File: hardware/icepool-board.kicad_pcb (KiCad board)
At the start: 4 copper layers, 152 x 96 mm, 120 parts, among them J1 USB_B_Micro, J10 Conn_02x08_Odd_Even, J11 Conn_02x08_Odd_Even, J12 Conn_02x08_Odd_Even, J13 Conn_02x08_Odd_Even, J14 Conn_02x08_Odd_Even, J15 Conn_02x08_Odd_Even, J16 Conn_02x08_Odd_Even, J17 Conn_02x08_Odd_Even, J18 Conn_02x08_Odd_Even, J19 Conn_02x08_Odd_Even, J2 Conn_01x02, J20 Conn_02x08_Odd_Even, J21 Conn_01x04, J3 PCIe_6pin, J4 Conn_02x08_Odd_Even, J5 Conn_02x08_Odd_Even, J6 Conn_02x08_Odd_Even, J7 Conn_02x08_Odd_Even, J8 Conn_02x08_Odd_Even, J9 Conn_02x08_Odd_Even, U1 FT232H, U2 AP7361C_SOT-89-5, U6 AP7361C_SOT-89-5, U7 AP7361C_SOT-89-5, U8 iCE40HX8K-BG121(121-Ball_caBG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, U9 AOZ2255LQI-30, X1 ASEM1-12.000MHZ, X2 ASEM1-12.000MHZ

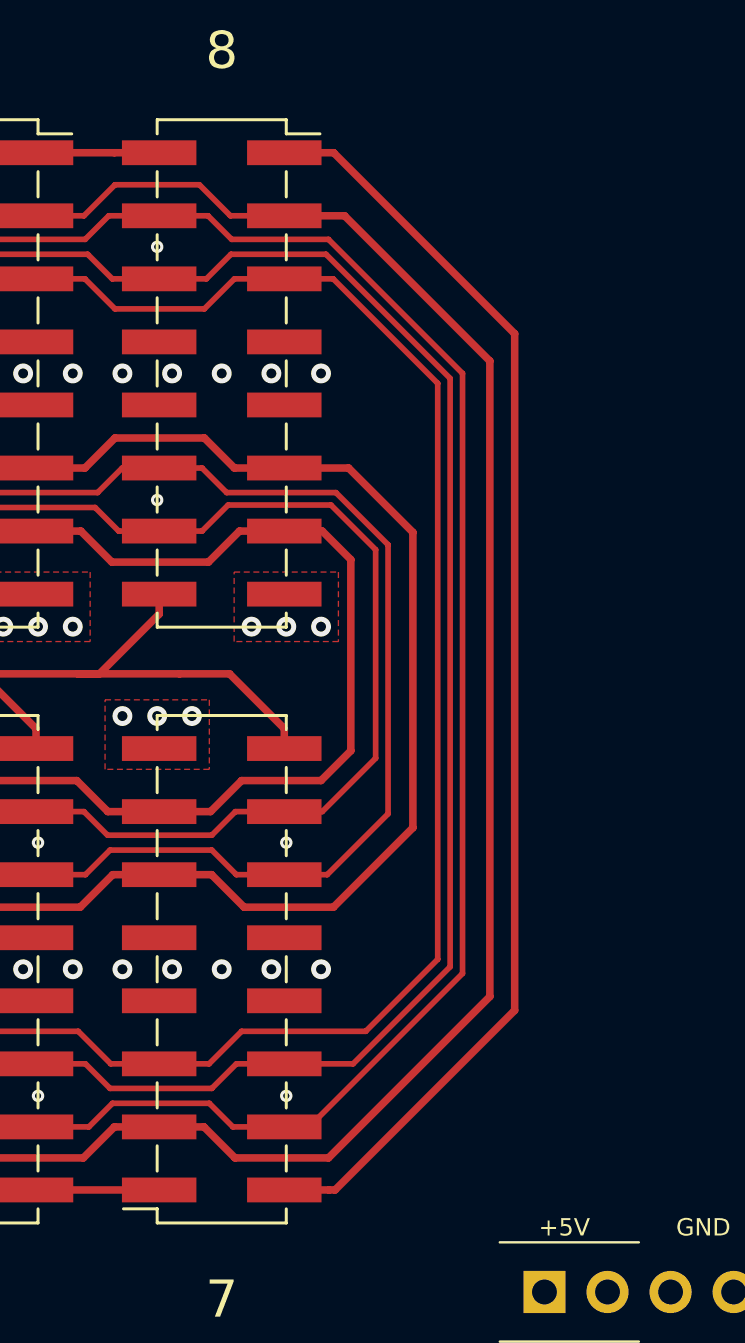
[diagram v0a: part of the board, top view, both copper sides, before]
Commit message: Spread out bus signals more uniformly.
Addresses issue #44.
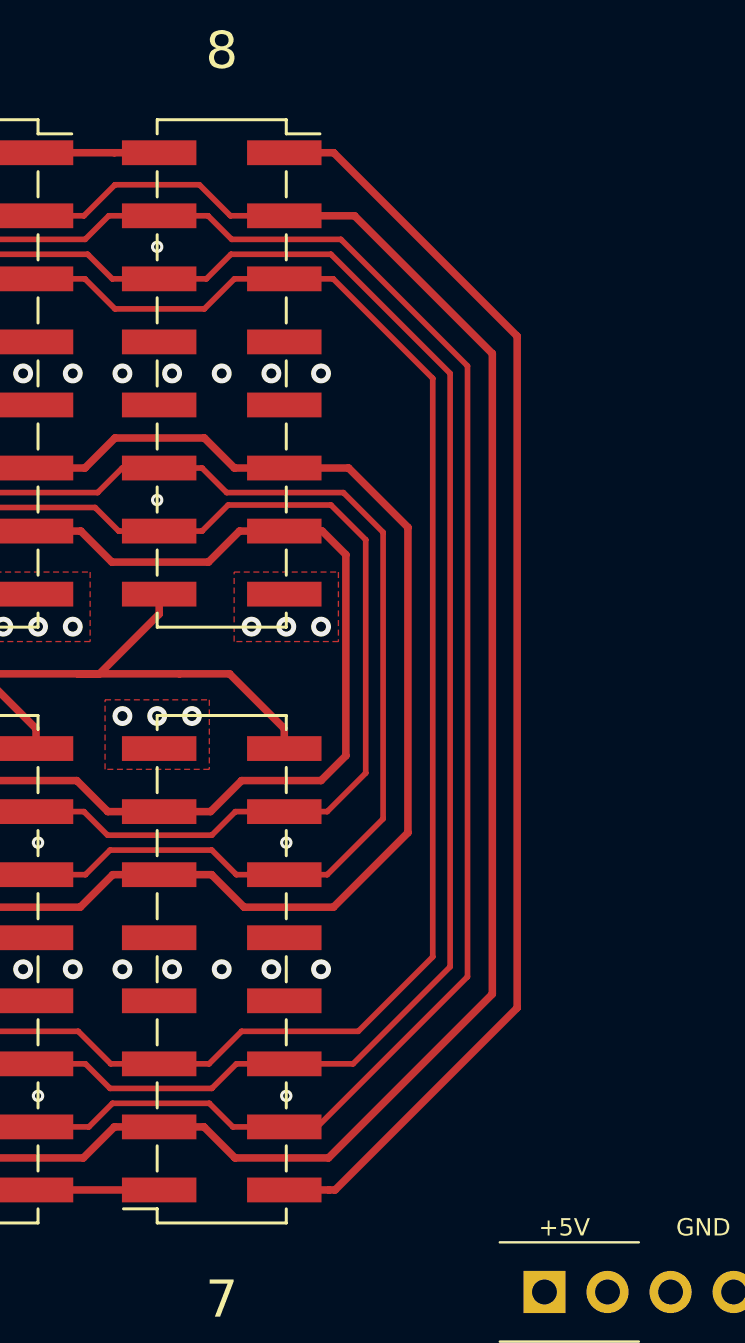
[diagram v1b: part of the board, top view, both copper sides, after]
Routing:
- net /icepool-motherboard/~RW: track 232.9 -> 233.6 mm
- net GND: vias 277 -> 287
- net (no net): vias 10 -> 0

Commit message: +silkscreen. Version++. +OSHW
Addresses issue #46.
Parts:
- added REF**: OSHW-Symbol_6.7x6mm_Copper, Symbol:OSHW-Symbol_6.7x6mm_Copper, B.Cu at (41.5, 85.2)
- added REF**: OSHW-Symbol_13.4x12mm_Copper, Symbol:OSHW-Symbol_13.4x12mm_Copper, F.Cu at (45.8, 72.8)
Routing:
- net +3V3: track 51.1 -> 53.7 mm
- net GND: vias 287 -> 290
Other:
- board text added: "icepool 2021.02 fourside.io"
- board text added: "icepool v2021.02 fourside.io"
- board text removed: "icepool 2021.01 fourside.io"

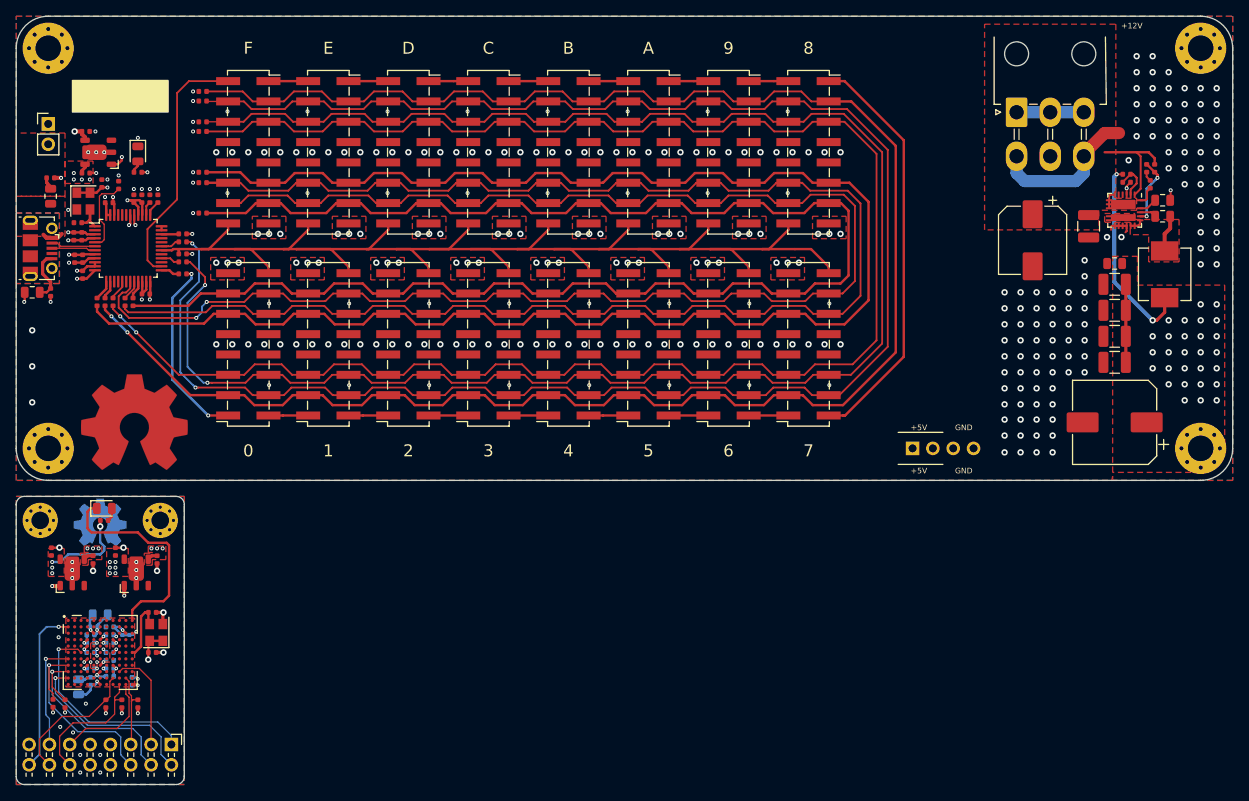
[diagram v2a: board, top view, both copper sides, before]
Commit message: Refactored for TPS62133 (5V, 3A) buck converter.
Changes motherboard dimensions. Changes motherboard stencil.

Addresses issue #42.
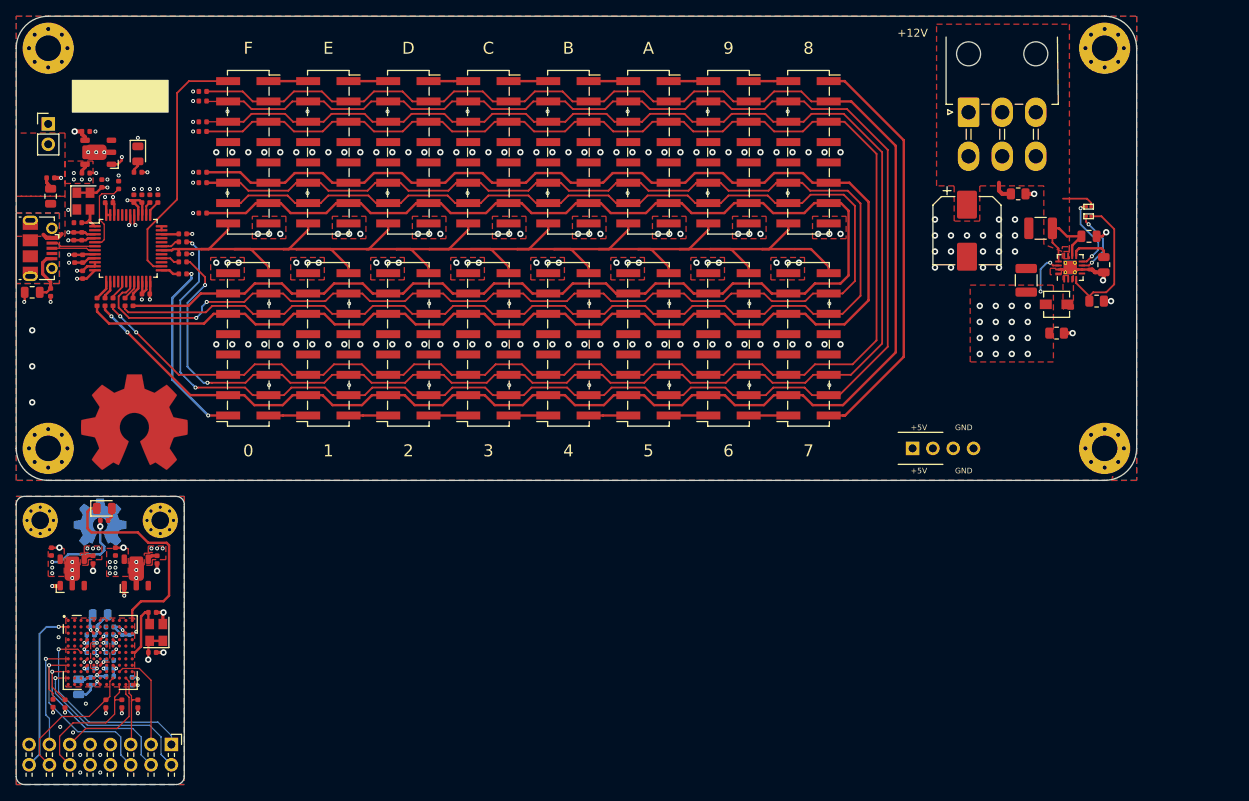
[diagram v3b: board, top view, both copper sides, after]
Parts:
- removed C40, C42: 0.1u, Capacitor_SMD:C_0805_2012Metric
- removed C43, C44, C45, C46: 22u, Capacitor_SMD:C_1210_3225Metric
- removed C47: 100u, Capacitor_SMD:CP_Elec_10x10
- removed C48: 0.1u, Capacitor_SMD:C_0402_1005Metric
- removed U9: AOZ2255LQI-30, jkiv-library:QFN-22L-EP2_4x4mm_P0.5mm
- added C15: 47u, Capacitor_SMD:CP_Elec_8x10, F.Cu at (149.8, 48.8)
- added JP2: FSW, jkiv-library:J_NO_0201_0603Metric, F.Cu at (165.0, 47.0)
- added JP3: FSW, jkiv-library:J_NO_0201_0603Metric, F.Cu at (165.0, 45.8)
- added U3: TPS62133, Package_DFN_QFN:VQFN-16-1EP_3x3mm_P0.5mm_EP1.68x1.68mm_ThermalVias, F.Cu at (162.7, 53.4)
- C37: value 0.1n -> 10u; footprint Capacitor_SMD:C_0402_1005Metric -> Capacitor_SMD:C_1210_3225Metric
- C38: value 22u -> 3.3u; footprint Capacitor_SMD:C_1210_3225Metric -> Capacitor_SMD:C_0805_2012Metric
- C39: value 47u -> 0.1u; footprint Capacitor_SMD:CP_Elec_8x10 -> Capacitor_SMD:C_0805_2012Metric
- C41: value 4.7u -> 22u; footprint Capacitor_SMD:C_0805_2012Metric -> Capacitor_SMD:C_1210_3225Metric
- L1: value 0.68u -> 2.2u; footprint Inductor_SMD:L_Vishay_IHLP-2525 -> Inductor_SMD:L_Vishay_IHLP-1212
- R21: value 620k -> 100k; footprint Resistor_SMD:R_0402_1005Metric -> Resistor_SMD:R_0805_2012Metric
- R22: value 220k -> 100k; footprint Resistor_SMD:R_0402_1005Metric -> Resistor_SMD:R_0805_2012Metric
- R23: value 30k -> 100k; footprint Resistor_SMD:R_0402_1005Metric -> Resistor_SMD:R_0805_2012Metric
- R25: value 1k -> 4.7k
- moved R23 20.8 mm to (161.0, 61.6)
- moved C41 19.8 mm to (157.2, 55.0), turned to 90 degrees
- moved R21 17.3 mm to (156.2, 44.2), turned to 0 degrees
- moved R22 16.3 mm to (166.0, 57.6), turned to 180 degrees
- moved C37 15.2 mm to (159.0, 48.5), turned to 180 degrees
- moved L1 14.0 mm to (161.0, 58.0), turned to 180 degrees
- moved H3 12.0 mm to (167.0, 76.0)
- moved H4 12.0 mm to (167.0, 26.0)
- moved C39 7.07 mm to (165.1, 49.5), turned to 0 degrees
- moved J3 6.00 mm to (150.0, 34.0)
- moved C38 5.16 mm to (166.9, 53.0)
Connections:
- C37 pad 1: Net-(C37-Pad1) -> +12V
- C38 pad 1: +12V -> Net-(C38-Pad1)
- C41 pad 1: Net-(C41-Pad1) -> +5V
- J1 pad 5: Net-(C9-Pad1) -> GND
- J1 pad 6: Net-(J1-Pad6) -> Net-(C9-Pad1)
- L1 pad 1: /icepool-motherboard/12V-5V Buck/LX -> /icepool-motherboard/12V-5V Buck/SW
- R21 pad 2: Net-(C37-Pad1) -> GND
- R22 pad 2: Net-(R22-Pad2) -> /icepool-motherboard/12V-5V Buck/PG
- R23 pad 1: Net-(R22-Pad2) -> +5V
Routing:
- net +5V: track 42.3 -> 14.1 mm, vias 87 -> 76
- net /icepool-motherboard/12V-5V Buck/PG: track 0.00 -> 17.6 mm
- net GND: track 56.7 -> 39.5 mm, vias 290 -> 199
- net /icepool-motherboard/12V-5V Buck/DEF: track 0.00 -> 9.51 mm, vias 0 -> 2
- net /icepool-motherboard/12V-5V Buck/FSW: track 0.00 -> 8.64 mm, vias 0 -> 2
- net Net-(C37-Pad1): track 8.43 -> 0.00 mm, vias 2 -> 0
- net /icepool-motherboard/12V-5V Buck/LX: track 6.36 -> 0.00 mm
- net +12V: track 23.9 -> 18.3 mm
- net Net-(C38-Pad1): track 0.00 -> 5.11 mm
- net Net-(R22-Pad2): track 4.79 -> 0.00 mm
- net Net-(C48-Pad1): track 2.43 -> 0.00 mm
- net Net-(C41-Pad1): track 2.29 -> 0.00 mm
- net Net-(C40-Pad1): track 2.08 -> 0.00 mm
- added copper zone on F.Cu, net /icepool-motherboard/12V-5V Buck/SW
- added copper zone on B.Cu, net Net-(C9-Pad1)
- added copper zone on F.Cu, net Net-(C9-Pad1)
- added copper zone on In1.Cu, net Net-(C9-Pad1)
- added copper zone on In2.Cu, net Net-(C9-Pad1)
- removed copper zone on F.Cu, net /icepool-motherboard/12V-5V Buck/LX
- removed copper zone on In2.Cu, net GND
- removed copper zone on B.Cu, net Net-(J1-Pad6)
- removed copper zone on F.Cu, net Net-(J1-Pad6)
- removed copper zone on In1.Cu, net Net-(J1-Pad6)
- removed copper zone on In2.Cu, net Net-(J1-Pad6)
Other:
- board size 152 x 96 mm -> 140 x 96 mm

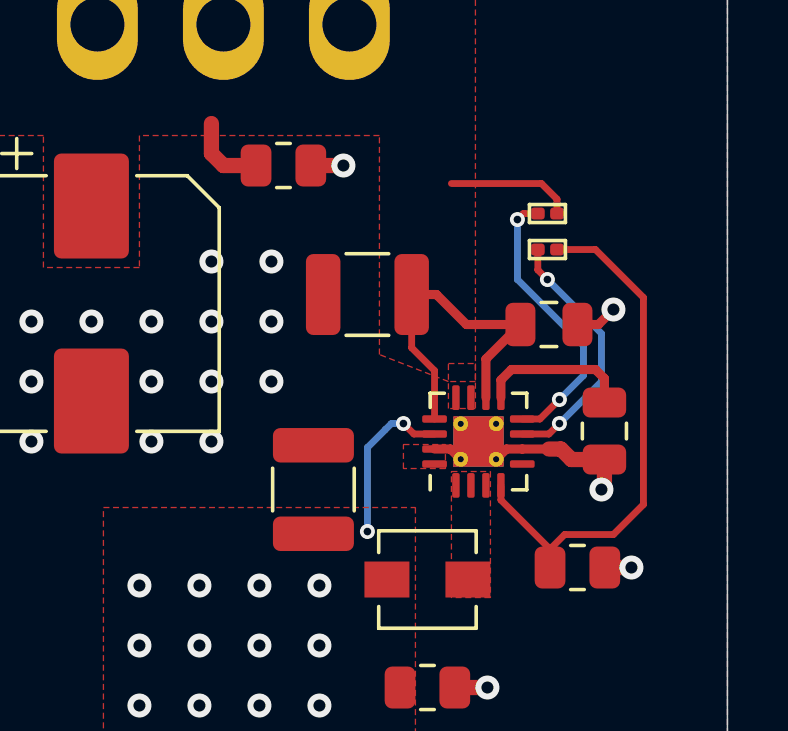
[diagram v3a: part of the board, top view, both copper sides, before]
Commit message: Added labels for DEF and FSW.
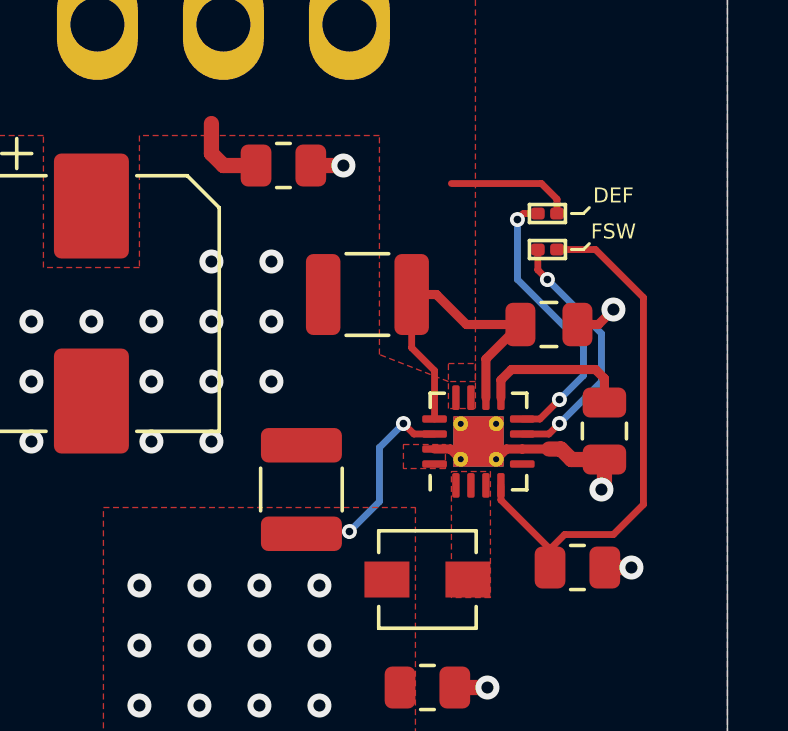
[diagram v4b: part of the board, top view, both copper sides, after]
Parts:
- moved C41 0.40 mm to (156.8, 55.0)
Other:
- board text added: "DEF"
- board text added: "FSW"
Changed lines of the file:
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@@
   (general
     (thickness 1.6)
-    (drawings 49)
-    (tracks 1592)
+    (drawings 55)
+    (tracks 1591)
     (zones 0)
     (modules 117)
@@
     (45 Margin user hide)
     (46 B.CrtYd user hide)
-    (47 F.CrtYd user hide)
+    (47 F.CrtYd user)
     (48 B.Fab user hide)
     (49 F.Fab user hide)
@@
     (user_trace_width 2.032)
     (trace_clearance 0.0889)
-    (zone_clearance 0.1016)
+    (zone_clearance 0.1524)
     (zone_45_only no)
     (trace_min 0.1016)
@@
   )
   (module Capacitor_SMD:C_1210_3225Metric (layer F.Cu)
-    (at 157.2 55 90)
+    (at 156.8 55 90)
     (descr "Capacitor SMD 1210 (3225 Metric), square (rectangular) end terminal, IPC_7351 nominal, (Body size source: IPC-SM-782 page 76, https://www.pcb-3d.com/wordpress/wp-content/uploads/ipc-sm-782a_amendment_1_and_2.pdf), generated with kicad-footprint-generator")
     (tags capacitor)
@@
     )
   )
+  (gr_line (start 166.2 47) (end 166.4 46.8) (layer F.SilkS) (width 0.1))
+  (gr_line (start 165.8 47) (end 166.2 47) (layer F.SilkS) (width 0.1))
+  (gr_line (start 166.2 45.8) (end 166.4 45.6) (layer F.SilkS) (width 0.1))
+  (gr_line (start 165.8 45.8) (end 166.2 45.8) (layer F.SilkS) (width 0.1))
+  (gr_text FSW (at 167.2 46.4) (layer F.SilkS)
+    (effects (font (size 0.5 0.5) (thickness 0.1)))
+  )
+  (gr_text DEF (at 167.2 45.2) (layer F.SilkS)
+    (effects (font (size 0.5 0.5) (thickness 0.1)))
+  )
   (gr_circle (center 161.1 55.5) (end 161.1 55.5) (layer F.SilkS) (width 0.5))
   (gr_poly (pts (xy 33 58.75) (xy 33.000001 72.75) (xy 31 72.75) (xy 31 58.750001)) (layer F.Mask) (width 0.1))
@@
   (segment (start 160.55 53.15) (end 160.2 52.8) (width 0.2286) (layer F.Cu) (net 10))
   (segment (start 161.2375 53.15) (end 160.55 53.15) (width 0.2286) (layer F.Cu) (net 10))
-  (segment (start 160.2 52.8) (end 159.8 52.8) (width 0.2286) (layer B.Cu) (net 10))
-  (segment (start 159.8 52.8) (end 159.6 53) (width 0.2286) (layer B.Cu) (net 10))
-  (via (at 159 56.4) (size 0.5) (drill 0.254) (layers F.Cu B.Cu) (net 10))
-  (segment (start 159 53.6) (end 159 56.4) (width 0.2286) (layer B.Cu) (net 10))
-  (segment (start 159.6 53) (end 159 53.6) (width 0.2286) (layer B.Cu) (net 10))
+  (via (at 158.4 56.4) (size 0.5) (drill 0.254) (layers F.Cu B.Cu) (net 10))
+  (segment (start 159.4 55.4) (end 158.4 56.4) (width 0.2286) (layer B.Cu) (net 10))
+  (segment (start 159.4 53.6) (end 159.4 55.4) (width 0.2286) (layer B.Cu) (net 10))
+  (segment (start 160.2 52.8) (end 159.4 53.6) (width 0.2286) (layer B.Cu) (net 10))
   (segment (start 35.4625 49.7) (end 34.8 49.7) (width 0.508) (layer F.Cu) (net 11))
   (segment (start 34.8 49.7) (end 34.4 49.3) (width 0.508) (layer F.Cu) (net 11))
@@
   (zone (net 2) (net_name +12V) (layer F.Cu) (hatch edge 0.508)
     (priority 2)
-    (connect_pads (clearance 0.254))
-    (min_thickness 0.254)
+    (connect_pads (clearance 0.1524))
+    (min_thickness 0.1524)
     (fill yes (arc_segments 32) (thermal_gap 0.127) (thermal_bridge_width 0.3048) (smoothing fillet) (radius 0.1))
     (polygon
@@
   (zone (net 10) (net_name +5V) (layer F.Cu) (hatch edge 0.508)
     (priority 2)
-    (connect_pads (clearance 0.254))
-    (min_thickness 0.254)
+    (connect_pads (clearance 0.1524))
+    (min_thickness 0.1524)
     (fill yes (arc_segments 32) (thermal_gap 0.127) (thermal_bridge_width 0.508) (smoothing fillet) (radius 0.1))
     (polygon
